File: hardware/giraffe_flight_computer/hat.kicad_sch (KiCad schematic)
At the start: 74 parts, among them U14 DS18B20, U19 SAM-M8Q

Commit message: More Schematic changes
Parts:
- removed C49: ?μF, symbol Device:C_Polarized_Small
- added NT1, NT2, NT3: NetTie, symbol Device:NetTie_2
- C11: renamed from C56; footprint (none) -> Capacitor_Tantalum_SMD:CP_EIA-3216-18_Kemet-A
- C18: renamed from C63; footprint (none) -> Capacitor_Tantalum_SMD:CP_EIA-7343-31_Kemet-D
- C19: renamed from C64; footprint (none) -> Capacitor_Tantalum_SMD:CP_EIA-3216-18_Kemet-A
- C6: renamed from C51; footprint (none) -> Capacitor_Tantalum_SMD:CP_EIA-3216-18_Kemet-A
- L1: renamed from L5; footprint (none) -> Inductor_SMD:L_Coilcraft_XAL4020-XXX
- LED1: value LED -> PWR; footprint (none) -> LED_SMD:LED_0603_1608Metric
- LED2: value ~ -> STATUS; footprint (none) -> giraffe_flight_computer_footprints:B36S3RGB LED
- U?: AVAILABILITY Good -> (none); Digikey https://www.digikey.com/short/pjf7tjwh -> (none); MF Bosch -> (none); MP BME280 -> (none); PACKAGE LGA-8 Bosch -> (none); PRICE 4.94 USD -> (none); STANDARD IPC-7351B -> (none)
- renumbered TP17 to TP1, TP18 to TP2, TP19 to TP3, TP20 to TP4, TP21 to TP5, U14 to U3, U19 to U8
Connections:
- net H_3V3: now also NT2.2; no longer R?.1
- net H_5V_HAT: now also NT3.1
- net H_GND: now also C?.1, C?.1, NT1.2
- new net -BATT: NT1.1
- new net 3V3: NT2.1, R?.1
- new net 5V: NT3.2

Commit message: Rev A Hat Complete
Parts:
- removed 1W? (x2): 1-Wire, giraffe_flight_computer_footprints:Molex-52745-0497, symbol Connector_Generic:Conn_01x03
- removed C? (x2): 0.1µF, Capacitor_SMD:C_0603_1608Metric, symbol Device:C_Small
- removed NT1, NT2, NT3: NetTie, symbol Device:NetTie_2
- removed Q?: DMG2305UX, Package_TO_SOT_SMD:SOT-23-3, symbol Simulation_SPICE:PMOS
- removed Q?: DMMT5401, Package_TO_SOT_SMD:SOT-23-6, symbol giraffe_symbols:DMMT5401
- removed R? (x4): ?, Resistor_SMD:R_0603_1608Metric, symbol Device:R_Small
- removed R?: 1k, Potentiometer_SMD:Potentiometer_Bourns_TC33X_Vertical, symbol Device:R_Trim
- removed R?: ?Ω, Resistor_SMD:R_0603_1608Metric, symbol Device:R_Small
- removed TP1, TP2, TP3, TP4, TP5: ~, symbol Connector:TestPoint_Alt
- removed U?: INA180A1, Package_TO_SOT_SMD:SOT-23-5, symbol giraffe_symbols:INA180A
- added C? (x2): 0.1µF, Capacitor_SMD:C_0603_1608Metric, symbol Device:C_Small
- added I2C?: 1W2, giraffe_flight_computer_footprints:Molex-52745-0497, symbol giraffe_symbols:Molex_4-pin_ribbon_connector
- added I2C?: 1W1, giraffe_flight_computer_footprints:Molex-52745-0497, symbol giraffe_symbols:Molex_4-pin_ribbon_connector
- added J10: BATT_C, Connector_PinHeader_1.00mm:PinHeader_1x03_P1.00mm_Vertical, symbol Connector_Generic:Conn_01x03
- added R? (x2): ?, Resistor_SMD:R_0603_1608Metric, symbol Device:R_Small
- added R?: 1k, Potentiometer_SMD:Potentiometer_Bourns_TC33X_Vertical, symbol giraffe_symbols:R_Potentiometer
- added TP3: GND, TestPoint:TestPoint_Keystone_5015_Micro-Minature, symbol Connector:TestPoint_Flag
- I2C?: value I²C -> PCM; footprint giraffe_flight_computer_footprints:Molex-52745-0497 -> Connector_PinHeader_1.27mm:PinHeader_1x04_P1.27mm_Vertical
- I2C?: symbol Connector_Generic:Conn_01x04 -> giraffe_symbols:Molex_4-pin_ribbon_connector
- U?: footprint SOIC127P600X175-8N -> giraffe_flight_computer_footprints:CAT24C32WI_GT3
- U?: footprint footprints:PSON65P250X250X100-8N -> giraffe_flight_computer_footprints:BME280
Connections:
- net 3V3 is gone; now on net H_3V3: R?.1
- net H_5V_HAT is gone; now on net H_5V: C18.1, C19.1, C?.1, C?.1, C?.2, R?.1, R?.1, U?.3 (V_In)
- net +BATT: now also C6.1, L1.1, R?.1, U?.1 (VIN), U?.2 (EN)
- net 1_WIRE: now also I2C?.2 (Pin_2), I2C?.2 (Pin_2)
- net H_3V3: now also C?.2, C?.2, I2C?.3 (Pin_3), I2C?.3 (Pin_3), I2C?.MP2 (Mount_Point)
- net H_GND: now also C?.1, C?.1, I2C?.1 (Pin_1), I2C?.1 (Pin_1), J10.1 (Pin_1), R?.2, TP3.1
- net at R?.1, U?.5 (FB): now also R?.1
- net H_5V: now reaches C11.1, R?.1, U?.8 (VOUT)
- net H_5V: now also J10.3 (Pin_3)
- net ADC.CH0: now reaches R?.1, R?.2, U?.5 (AIN0)
- net ADC.CH2: now reaches R?.1, R?.2, U?.7 (AIN2)
- net ADC.CH3: now reaches R?.1, R?.2, U?.8 (AIN3)
- net BOOST_SW: now reaches L1.2, U?.7 (SW)
- net ADC.CH1: now reaches U?.6 (AIN1)
- net ADC.CH1: now also R?.1, R?.2
- net at R?.2: now also R?.2
- new net: J10.2 (Pin_2), R?.1
- no-connect marks 7 -> 11
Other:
- note removed: "Reverse Polarity Protection"
- note removed: "eevblog.com/forum/projects /how-does-the-zvd-circuit-work/"
- moved on the sheet: C11, R?

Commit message: status led data sharing
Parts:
- LED1: value PWR -> SML-D12M8WT86
- LED2: value STATUS -> B36S3RGB-F6C0001HOU1930
- R1: renamed from R?; value ?Ω -> 56Ω
- R6: renamed from R?; value ?Ω -> 270Ω
- R7, R8: renamed from R?; value ?Ω -> 360Ω
- gave numbers to parts that had none: 45

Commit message: buck converter planning
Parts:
- R10: value ? -> 2.2k
- R9: value ? -> 6.8k
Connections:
- net ADC_V_REF: now reaches C?.1, U7.1 (REF), U9.1 (V_Out)

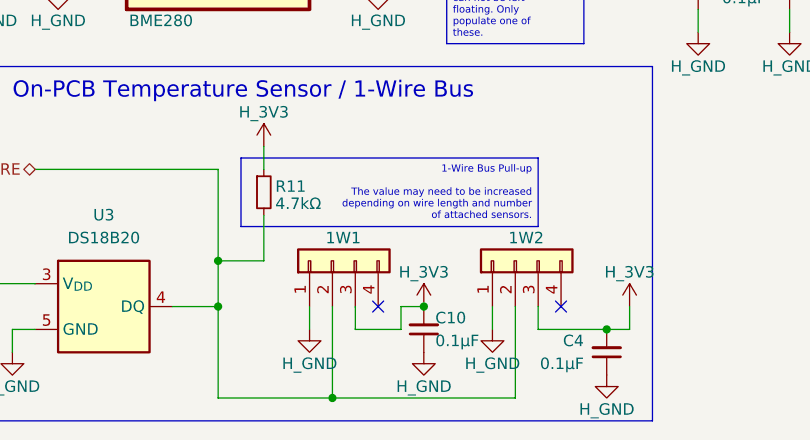
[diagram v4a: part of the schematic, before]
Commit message: first round of updates to telemetry board
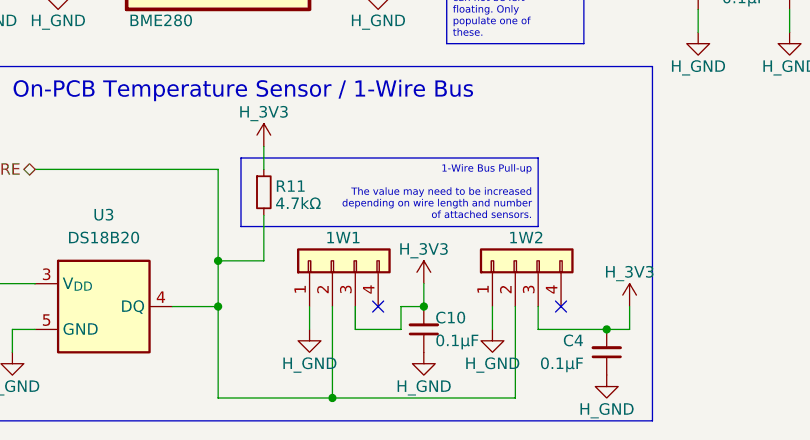
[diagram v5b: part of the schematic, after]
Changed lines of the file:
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@@
 	)
 	(junction
-		(at 149.86 185.42)
+		(at 144.78 147.32)
 		(diameter 0)
 		(color 0 0 0 0)
 	)
 	(junction
-		(at 144.78 147.32)
+		(at 248.92 137.16)
 		(diameter 0)
 		(color 0 0 0 0)
 	)
 	(junction
-		(at 248.92 137.16)
+		(at 134.62 76.2)
 		(diameter 0)
 		(color 0 0 0 0)
 	)
 	(junction
-		(at 134.62 76.2)
+		(at 149.86 185.42)
 		(diameter 0)
 		(color 0 0 0 0)
@@
 	(wire
 		(pts
+			(xy 147.32 185.42) (xy 147.32 187.96)
+		)
+		(stroke
+			(width 0)
+			(type default)
+		)
+	)
+	(wire
+		(pts
 			(xy 71.12 152.4) (xy 73.66 152.4)
 		)
@@
 	(wire
 		(pts
+			(xy 149.86 182.88) (xy 149.86 185.42)
+		)
+		(stroke
+			(width 0)
+			(type default)
+		)
+	)
+	(wire
+		(pts
 			(xy 228.6 96.52) (xy 228.6 121.92)
 		)
@@
 	(wire
 		(pts
-			(xy 109.22 104.14) (xy 109.22 109.22)
+			(xy 142.24 187.96) (xy 142.24 185.42)
 		)
 		(stroke
@@
 	(wire
 		(pts
-			(xy 243.84 83.82) (xy 248.92 83.82)
+			(xy 109.22 104.14) (xy 109.22 109.22)
 		)
 		(stroke
@@
 	(wire
 		(pts
-			(xy 193.04 99.06) (xy 195.58 99.06)
+			(xy 243.84 83.82) (xy 248.92 83.82)
 		)
 		(stroke
@@
 	(wire
 		(pts
-			(xy 147.32 187.96) (xy 147.32 185.42)
+			(xy 193.04 99.06) (xy 195.58 99.06)
 		)
 		(stroke
@@
 	(wire
 		(pts
-			(xy 147.32 185.42) (xy 149.86 185.42)
+			(xy 269.24 96.52) (xy 269.24 99.06)
 		)
 		(stroke
@@
 	(wire
 		(pts
-			(xy 269.24 96.52) (xy 269.24 99.06)
+			(xy 127 195.58) (xy 139.7 195.58)
 		)
 		(stroke
@@
 	(wire
 		(pts
-			(xy 127 195.58) (xy 139.7 195.58)
+			(xy 50.8 116.84) (xy 50.8 119.38)
 		)
 		(stroke
@@
 	(wire
 		(pts
-			(xy 50.8 116.84) (xy 50.8 119.38)
+			(xy 96.52 30.48) (xy 96.52 33.02)
 		)
 		(stroke
@@
 	(wire
 		(pts
-			(xy 96.52 30.48) (xy 96.52 33.02)
+			(xy 264.16 30.48) (xy 264.16 33.02)
 		)
 		(stroke
@@
 	(wire
 		(pts
-			(xy 264.16 30.48) (xy 264.16 33.02)
+			(xy 152.4 40.64) (xy 154.94 40.64)
 		)
 		(stroke
@@
 	(wire
 		(pts
-			(xy 152.4 40.64) (xy 154.94 40.64)
+			(xy 175.26 134.62) (xy 180.34 134.62)
 		)
 		(stroke
@@
 	(wire
 		(pts
-			(xy 175.26 134.62) (xy 180.34 134.62)
+			(xy 149.86 185.42) (xy 147.32 185.42)
 		)
 		(stroke
@@
 	(wire
 		(pts
-			(xy 142.24 185.42) (xy 142.24 187.96)
-		)
-		(stroke
-			(width 0)
-			(type default)
-		)
-	)
-	(wire
-		(pts
 			(xy 35.56 68.58) (xy 35.56 71.12)
 		)
@@
 	(wire
 		(pts
+			(xy 147.32 187.96) (xy 142.24 187.96)
+		)
+		(stroke
+			(width 0)
+			(type default)
+		)
+	)
+	(wire
+		(pts
 			(xy 264.16 149.86) (xy 269.24 149.86)
 		)
@@
 	(wire
 		(pts
-			(xy 142.24 187.96) (xy 147.32 187.96)
-		)
-		(stroke
-			(width 0)
-			(type default)
-		)
-	)
-	(wire
-		(pts
 			(xy 152.4 50.8) (xy 152.4 53.34)
 		)
@@
 	(symbol
 		(lib_id "giraffe_symbols:H_3V3")
-		(at 149.86 185.42 0)
+		(at 149.86 182.88 0)
 		(unit 1)
 		(exclude_from_sim no)
@@
 		(dnp no)
 		(property "Reference" "#PWR035"
-			(at 149.86 189.23 0)
+			(at 149.86 186.69 0)
 			(effects
 				(font
@@
 		)
 		(property "Value" "H_3V3"
-			(at 149.86 181.61 0)
+			(at 149.86 179.07 0)
 			(effects
 				(font
@@
 		)
 		(property "Footprint" ""
-			(at 149.86 185.42 0)
+			(at 149.86 182.88 0)
 			(effects
 				(font
@@
 		)
 		(property "Datasheet" ""
-			(at 149.86 185.42 0)
+			(at 149.86 182.88 0)
 			(effects
 				(font
@@
 		)
 		(property "Description" ""
-			(at 149.86 185.42 0)
+			(at 149.86 182.88 0)
 			(effects
 				(font

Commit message: reorganization
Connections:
- net H_3V3: no longer 1W1.MP2 (Mount_Point)
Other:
- note added: "3V3 supply TODO"
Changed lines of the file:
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@@
 		)
 	)
+	(text "3V3 supply TODO"
+		(exclude_from_sim no)
+		(at 186.055 49.53 0)
+		(effects
+			(font
+				(size 1.8 1.8)
+			)
+			(justify left bottom)
+		)
+	)
 	(text "Boost Converter"
 		(exclude_from_sim no)
@@
 	)
 	(symbol
+		(lib_id "giraffe_symbols:H_3V3")
+		(at 194.31 54.61 0)
+		(unit 1)
+		(exclude_from_sim no)
+		(in_bom yes)
+		(on_board yes)
+		(dnp no)
+		(property "Reference" "#PWR061"
+			(at 194.31 58.42 0)
+			(effects
+				(font
+					(size 1.27 1.27)
+				)
+				(hide yes)
+			)
+		)
+		(property "Value" "H_3V3"
+			(at 194.31 50.8 0)
+			(effects
+				(font
+					(size 1.27 1.27)
+				)
+			)
+		)
+		(property "Footprint" ""
+			(at 194.31 54.61 0)
+			(effects
+				(font
+					(size 1.27 1.27)
+				)
+				(hide yes)
+			)
+		)
+		(property "Datasheet" ""
+			(at 194.31 54.61 0)
+			(effects
+				(font
+					(size 1.27 1.27)
+				)
+				(hide yes)
+			)
+		)
+		(property "Description" ""
+			(at 194.31 54.61 0)
+			(effects
+				(font
+					(size 1.27 1.27)
+				)
+				(hide yes)
+			)
+		)
+		(pin "1"
+		)
+		(instances
+			(project "giraffe_flight_computer"
+				(path "/8b6d32d3-7736-4ef0-bfd7-9f676eec710d/7384c1b4-69d8-435f-8d37-4f0768f54f3f"
+					(reference "#PWR061")
+					(unit 1)
+				)
+			)
+		)
+	)
+	(symbol
 		(lib_id "Device:C_Small")
 		(at 78.74 157.48 180)
@@
 	)
 	(symbol
-		(lib_name "Molex_4-pin_ribbon_connector_2")
 		(lib_id "giraffe_symbols:Molex_4-pin_ribbon_connector")
 		(at 160.02 180.34 90)
@@
 			)
 		)
-		(property "Description" ""
+		(property "Description" "Generic connector, single row, 01x04, script generated (kicad-library-utils/schlib/autogen/connector/)"
 			(at 160.02 180.34 0)
 			(effects
@@
 	)
 	(symbol
-		(lib_name "Molex_4-pin_ribbon_connector_1")
 		(lib_id "giraffe_symbols:Molex_4-pin_ribbon_connector")
 		(at 139.7 180.34 90)
@@
 			)
 		)
-		(property "Description" ""
+		(property "Description" "Generic connector, single row, 01x04, script generated (kicad-library-utils/schlib/autogen/connector/)"
 			(at 139.7 180.34 0)
 			(effects
@@
 	)
 	(symbol
+		(lib_id "power:PWR_FLAG")
+		(at 194.31 54.61 0)
+		(mirror x)
+		(unit 1)
+		(exclude_from_sim no)
+		(in_bom yes)
+		(on_board yes)
+		(dnp no)
+		(property "Reference" "#FLG07"
+			(at 194.31 56.515 0)
+			(effects
+				(font
+					(size 1.27 1.27)
+				)
+				(hide yes)
+			)
+		)
+		(property "Value" "PWR_FLAG"
+			(at 200.66 55.88 0)
+			(effects
+				(font
+					(size 1.27 1.27)
+				)
+			)
+		)
+		(property "Footprint" ""
+			(at 194.31 54.61 0)
+			(effects
+				(font
+					(size 1.27 1.27)
+				)
+				(hide yes)
+			)
+		)
+		(property "Datasheet" "~"
+			(at 194.31 54.61 0)
+			(effects
+				(font
+					(size 1.27 1.27)
+				)
+				(hide yes)
+			)
+		)
+		(property "Description" "Special symbol for telling ERC where power comes from"
+			(at 194.31 54.61 0)
+			(effects
+				(font
+					(size 1.27 1.27)
+				)
+				(hide yes)
+			)
+		)
+		(pin "1"
+		)
+		(instances
+			(project "giraffe_flight_computer"
+				(path "/8b6d32d3-7736-4ef0-bfd7-9f676eec710d/7384c1b4-69d8-435f-8d37-4f0768f54f3f"
+					(reference "#FLG07")
+					(unit 1)
+				)
+			)
+		)
+	)
+	(symbol
 		(lib_id "Device:C_Small")
 		(at 71.12 157.48 180)
@@
 			)
 		)
-		(property "Description" ""
+		(property "Description" "Generic connector, single row, 01x04, script generated (kicad-library-utils/schlib/autogen/connector/)"
 			(at 127 114.3 0)
 			(effects

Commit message: Packages, complete PCBs, Map, Install Structure
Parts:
- removed C11, C19, C6: 10μF, Capacitor_Tantalum_SMD:CP_EIA-3216-18_Kemet-A, symbol Device:C_Polarized_Small
- removed C18: 100μF, Capacitor_Tantalum_SMD:CP_EIA-7343-31_Kemet-D, symbol Device:C_Polarized_Small
- removed J10: BATT_C, Connector_PinHeader_1.00mm:PinHeader_1x03_P1.00mm_Vertical, symbol Connector_Generic:Conn_01x03
- removed J7: ~, Connector_PinHeader_1.00mm:PinHeader_1x04_P1.00mm_Vertical, symbol Connector_Generic:Conn_01x04
- removed L1: 0.47uH, Inductor_SMD:L_Coilcraft_XAL4020-XXX, symbol Device:L_Small
- removed PCM1: PCM, Connector_PinHeader_1.27mm:PinHeader_1x04_P1.27mm_Vertical, symbol Connector_Generic:Conn_01x04
- removed R12, R13, R22, R23: ?, Resistor_SMD:R_0603_1608Metric, symbol Device:R_Small
- removed R15: 21.5k, Resistor_SMD:R_0603_1608Metric, symbol Device:R_Small
- removed R16: 1k, Potentiometer_SMD:Potentiometer_Bourns_TC33X_Vertical, symbol giraffe_symbols:R_Potentiometer
- removed R17: 3k, Resistor_SMD:R_0603_1608Metric, symbol Device:R_Small
- removed U4: TPS61033, Package_TO_SOT_SMD:SOT-583-8, symbol giraffe_symbols:TPS61033
- removed U7: MAX11615, Package_SO:QSOP-16_3.9x4.9mm_P0.635mm, symbol giraffe_symbols:MAX1161x
- added C1, C56, C57: 0.1µF, Capacitor_SMD:C_0603_1608Metric, symbol Device:C_Small
- added C11: 10uf, Capacitor_SMD:C_1206_3216Metric, symbol Device:C_Small
- added C19, C58, C59: 22µF, Capacitor_SMD:C_1210_3225Metric, symbol Device:C_Small
- added C49, C50: 1uf, Capacitor_SMD:C_0805_2012Metric, symbol Device:C_Small
- added C55: 10µF, Capacitor_SMD:C_1206_3216Metric, symbol Device:C_Small
- added C6: C_Small, Capacitor_SMD:C_0402_1005Metric, symbol Device:C_Small
- added C60: 75pf, Capacitor_SMD:C_0603_1608Metric, symbol Device:C
- added L6: 10uH, giraffe_flight_computer_footprints:IND_SRU1048-100Y, symbol Device:L
- added R16: R_Small, Resistor_SMD:R_0402_1005Metric, symbol Device:R_Small
- added R44: 0.01Ω, Resistor_SMD:R_1206_3216Metric, symbol Device:R_Small
- added R48: 49, Resistor_SMD:R_0603_1608Metric, symbol Device:R
- added R49: 100k, Resistor_SMD:R_0603_1608Metric, symbol Device:R
- added R50: 13.3k, Resistor_SMD:R_0603_1608Metric, symbol Device:R
- added TP17: TestPoint, TestPoint:TestPoint_Pad_D1.0mm, symbol Connector:TestPoint
- added U13: TPS54302, Package_TO_SOT_SMD:SOT-23-6, symbol Regulator_Switching:TPS54302
- added U4: MAX11613, giraffe_flight_computer_footprints:SOP65P490X110-8N, symbol Analog_ADC:MAX11613
- added U6: INA180A3, Package_TO_SOT_SMD:SOT-23-5, symbol Amplifier_Current:INA180A3
- added U7: TLV75533PDBV, Package_TO_SOT_SMD:SOT-23-5, symbol Regulator_Linear:TLV75533PDBV
- 1W1, 1W2: footprint giraffe_flight_computer_footprints:Molex-52745-0497 -> giraffe_flight_computer_footprints:CONN_5037630000-SD_03_MOL
- C17, C21, C22: renamed from C?; now not fitted
- I2C1: footprint giraffe_flight_computer_footprints:Molex-52745-0497 -> giraffe_flight_computer_footprints:CONN_5037630000-SD_04_MOL
- R10, R2, R3, R6, R7, R8, R9: footprint Resistor_SMD:R_0603_1608Metric -> Resistor_SMD:R_0402_1005Metric
- U9: now not fitted
- gave numbers to parts that had none: 1
- renumbered C1 to C18
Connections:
- net +BATT: now also R44.1, U6.3 (+)
- net ADC.CH0: now also R2.2, R3.1, U4.1 (AIN0); no longer R10.1, R9.2
- net ADC.CH1: now also R10.1, R9.2, U4.2 (AIN1); no longer R2.2, R3.1
- net ADC.CH2: now also C6.1, R16.2, U4.3 (AIN2)
- net ADC_V_REF: now also U4.4 (AIN3/REF)
- net H_3V3: now also C1.1, C50.2, TP17.1, U4.8 (Vdd), U6.5 (V+), U7.5 (OUT)
- net H_5V: now also C11.2, C49.2, C58.1, C59.1, L6.1, R48.1, U7.1 (IN), U7.3 (EN)
- net H_GND: now also C1.2, C11.1, C19.2, C49.1, C50.1, C55.2, C56.2, C58.2, C59.2, C6.2, R50.2, U13.1 (GND), U4.7 (GND), U6.2 (GND), U7.2 (GND)
- net I2C0.SCL: now also I2C1.4 (Pin_4), U4.5 (SCL); no longer I2C1.3 (Pin_3)
- net I2C0.SDA: now also I2C1.3 (Pin_3), U4.6 (SDA); no longer I2C1.4 (Pin_4)
- net BAT_BALANCE: now reaches R2.1
- new net: C57.1, U13.6 (BOOT)
- new net: C57.2, L6.2, U13.2 (SW)
- new net: R16.1, U6.1
- new net: C60.1, R48.2, R49.1
- new net: C60.2, R49.2, R50.1, U13.4 (FB)
- new net BAT_SENSED: C19.1, C55.1, C56.1, R44.2, U13.3 (VIN), U6.4 (-)
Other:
- note added: "RP2040 3V3 LDO"
- note removed: "Boost Converter"
- note removed: "Current Sensor"
- moved on the sheet: C18, C20, R10, R2, R3, R4, R5, R9, U1
